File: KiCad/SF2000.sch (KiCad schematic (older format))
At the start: 24 parts, among them J1 Conn_2Rows-86Pins_even_odd, J2 Conn_01x02, U1 LM1117-3.3, U2 TPS73643DBV, U3 SN74CBT16211, U4 SN74CBT16211, U5 SN74CBT16211, U6 SN74AUP1T87DCKR

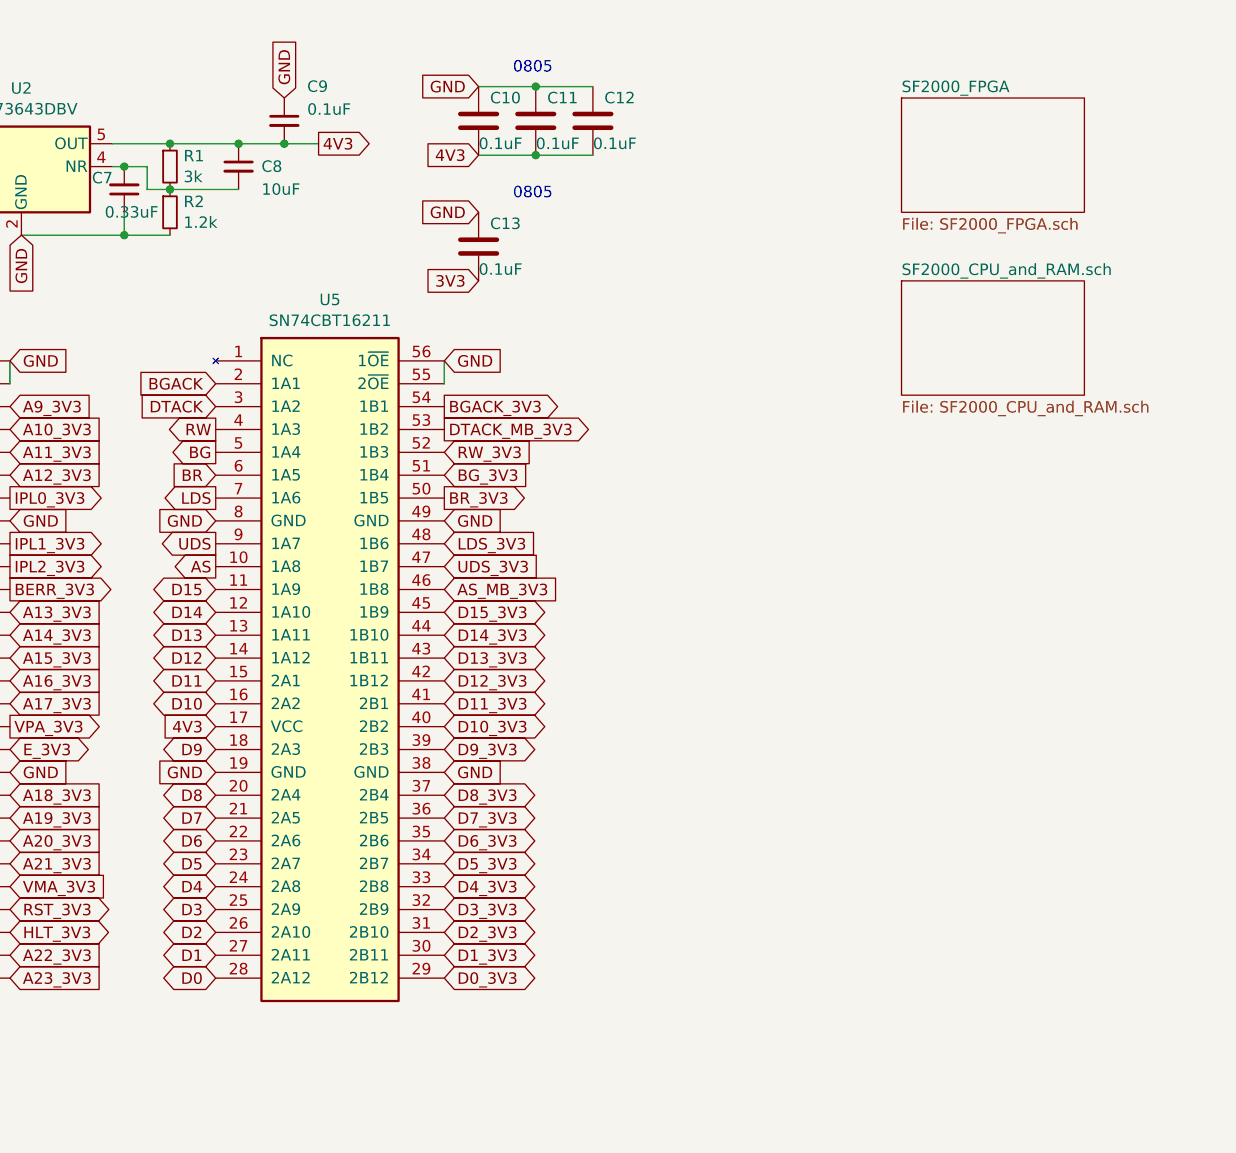
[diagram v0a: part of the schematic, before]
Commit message: reconnected SRAMs and rerouted, and added a lot of caps
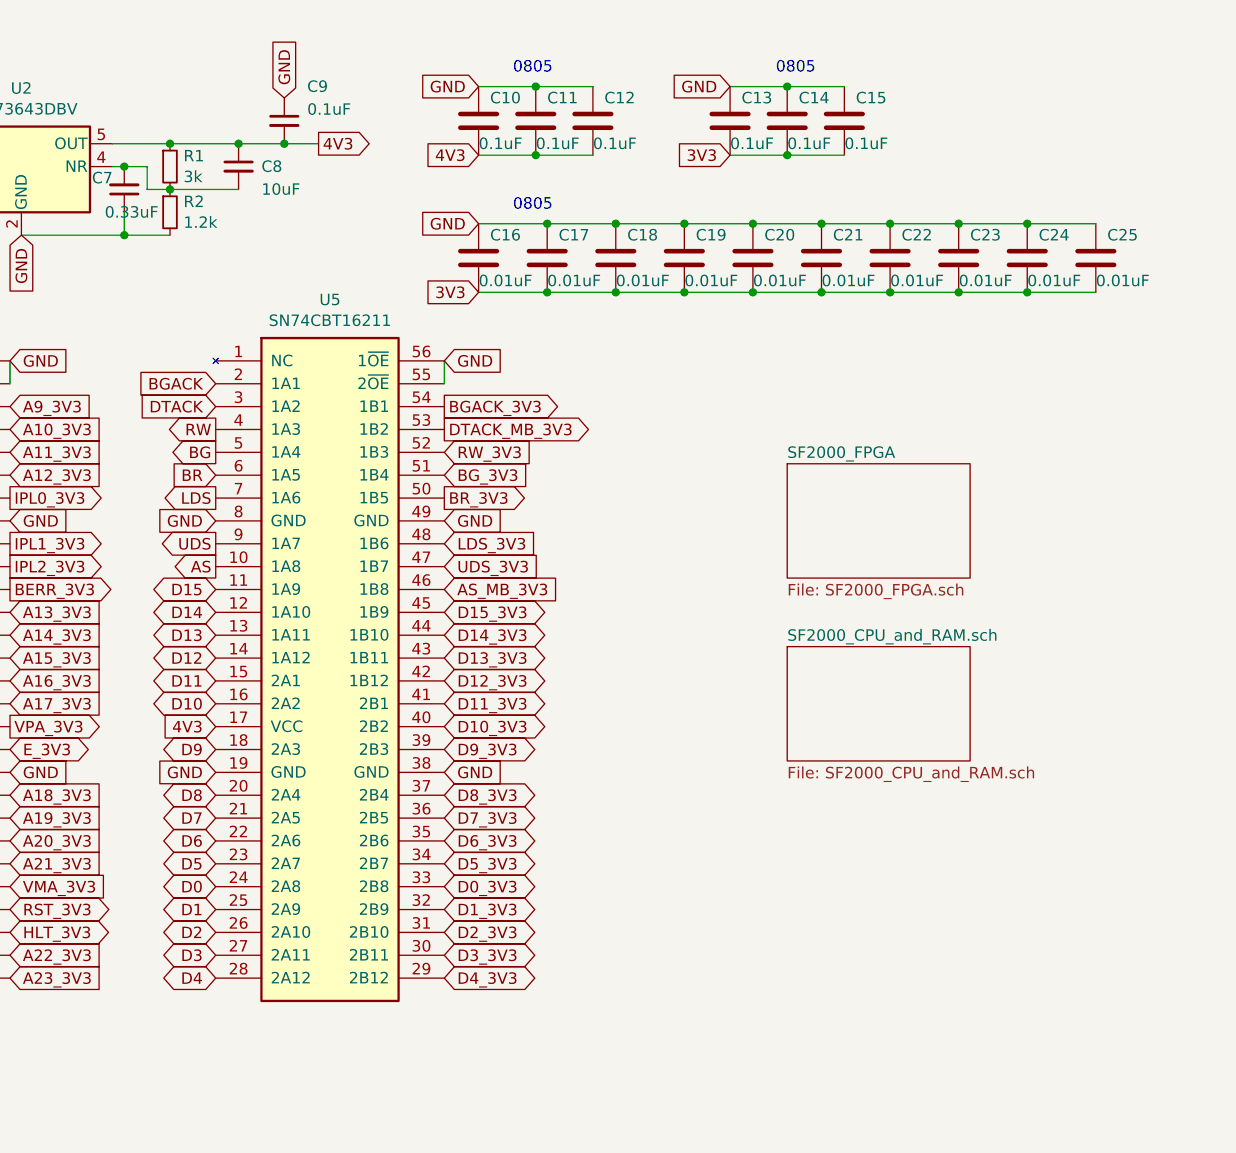
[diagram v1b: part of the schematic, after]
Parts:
- added C14, C15: 0.1uF, Capacitor_SMD:C_0805_2012Metric_Pad1.15x1.40mm_HandSolder, symbol Device:C
- added C16, C17, C18, C19, C20, C21, C22, C23, C24, C25: 0.01uF, Capacitor_SMD:C_0805_2012Metric_Pad1.15x1.40mm_HandSolder, symbol Device:C
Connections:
- net 3V3: now also C14.2, C15.2, C16.2, C17.2, C18.2, C19.2, C20.2, C21.2, C22.2, C23.2, C24.2, C25.2
- net D0: now also U5.24 (2A8); no longer U5.28 (2A12)
- net D0_3V3: now also U5.33 (2B8); no longer U5.29 (2B12)
- net D1: now also U5.25 (2A9); no longer U5.27 (2A11)
- net D1_3V3: now also U5.32 (2B9); no longer U5.30 (2B11)
- net D3: now also U5.27 (2A11); no longer U5.25 (2A9)
- net D3_3V3: now also U5.30 (2B11); no longer U5.32 (2B9)
- net D4: now also U5.28 (2A12); no longer U5.24 (2A8)
- net D4_3V3: now also U5.29 (2B12); no longer U5.33 (2B8)
- net GND: now also C14.1, C15.1, C16.1, C17.1, C18.1, C19.1, C20.1, C21.1, C22.1, C23.1, C24.1, C25.1
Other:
- moved on the sheet: C13
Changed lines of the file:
@@
 Text GLabel 6250 2850 0    50   Output ~ 0
 AS
-Text GLabel 6250 4650 0    50   BiDi ~ 0
+Text GLabel 6250 4250 0    50   BiDi ~ 0
 D0
 Text GLabel 6250 3450 0    50   BiDi ~ 0
 D10
-Text GLabel 6250 4550 0    50   BiDi ~ 0
+Text GLabel 6250 4350 0    50   BiDi ~ 0
 D1
 Text GLabel 6250 3650 0    50   BiDi ~ 0
@@
 Text GLabel 6250 3850 0    50   BiDi ~ 0
 D8
-Text GLabel 6250 4350 0    50   BiDi ~ 0
+Text GLabel 6250 4550 0    50   BiDi ~ 0
 D3
 Text GLabel 6250 3950 0    50   BiDi ~ 0
 D7
-Text GLabel 6250 4250 0    50   BiDi ~ 0
+Text GLabel 6250 4650 0    50   BiDi ~ 0
 D4
 Text GLabel 6250 4050 0    50   BiDi ~ 0
@@
 Text GLabel 2600 5400 0    50   Input ~ 0
 CCK_3V3
-Text GLabel 7400 1300 0    50   Input ~ 0
-GND
-Text GLabel 7400 1600 0    50   Input ~ 0
-3V3
-$Comp
-L Device:C C13
-U 1 1 620B176A
-P 7400 1450
-F 0 "C13" H 7450 1550 50  0000 L CNN
-F 1 "0.1uF" H 7400 1350 50  0000 L CNN
-F 2 "Capacitor_SMD:C_0805_2012Metric_Pad1.15x1.40mm_HandSolder" H 7438 1300 50  0001 C CNN
-F 3 "~" H 7400 1450 50  0001 C CNN
-	1    7400 1450
-	1    0    0    -1
-$EndComp
-Text Notes 7550 1250 0    50   ~ 0
-0805
 NoConn ~ 3550 2150
 NoConn ~ 3550 2250
@@
 CFGOUT_3V3
 $Sheet
-S 9250 800  800  500
+S 8750 2400 800  500
 U 620D263D
 F0 "SF2000_FPGA" 50
@@
 E_3V3
 $Sheet
-S 9250 1600 800  500
+S 8750 3200 800  500
 U 621DFEC4
 F0 "SF2000_CPU_and_RAM.sch" 50
@@
 Text GLabel 7250 2250 2    50   Output ~ 0
 DTACK_MB_3V3
-Text GLabel 7250 4650 2    50   BiDi ~ 0
+Text GLabel 7250 4250 2    50   BiDi ~ 0
 D0_3V3
-Text GLabel 7250 4550 2    50   BiDi ~ 0
+Text GLabel 7250 4350 2    50   BiDi ~ 0
 D1_3V3
 Text GLabel 7250 4450 2    50   BiDi ~ 0
 D2_3V3
-Text GLabel 7250 4350 2    50   BiDi ~ 0
+Text GLabel 7250 4550 2    50   BiDi ~ 0
 D3_3V3
-Text GLabel 7250 4250 2    50   BiDi ~ 0
+Text GLabel 7250 4650 2    50   BiDi ~ 0
 D4_3V3
 Text GLabel 7250 4150 2    50   BiDi ~ 0
@@
 LDS_3V3
 NoConn ~ 3550 3550
+Text Notes 8700 700  0    50   ~ 0
+0805
+Text GLabel 7400 1650 0    50   Input ~ 0
+3V3
+Text GLabel 7400 1350 0    50   Input ~ 0
+GND
+Text GLabel 8500 1050 0    50   Input ~ 0
+3V3
+Text GLabel 8500 750  0    50   Input ~ 0
+GND
+$Comp
+L Device:C C13
+U 1 1 620B176A
+P 8500 900
+F 0 "C13" H 8550 1000 50  0000 L CNN
+F 1 "0.1uF" H 8500 800 50  0000 L CNN
+F 2 "Capacitor_SMD:C_0805_2012Metric_Pad1.15x1.40mm_HandSolder" H 8538 750 50  0001 C CNN
+F 3 "~" H 8500 900 50  0001 C CNN
+	1    8500 900
+	1    0    0    -1
+$EndComp
+Wire Wire Line
+	9200 1650 9500 1650
+Connection ~ 9200 1650
+Wire Wire Line
+	8900 1650 9200 1650
+Connection ~ 8900 1650
+Wire Wire Line
+	8600 1650 8900 1650
+Connection ~ 8600 1650
+Connection ~ 8300 1650
+Wire Wire Line
+	8300 1650 8600 1650
+Wire Wire Line
+	9200 1350 9500 1350
+Connection ~ 9200 1350
+Wire Wire Line
+	8900 1350 9200 1350
+Connection ~ 8900 1350
+Wire Wire Line
+	8600 1350 8900 1350
+Connection ~ 8600 1350
+Connection ~ 8300 1350
+Wire Wire Line
+	8300 1350 8600 1350
+$Comp
+L Device:C C17
+U 1 1 623684C1
+P 7700 1500
+F 0 "C17" H 7750 1600 50  0000 L CNN
+F 1 "0.01uF" H 7700 1400 50  0000 L CNN
+F 2 "Capacitor_SMD:C_0805_2012Metric_Pad1.15x1.40mm_HandSolder" H 7738 1350 50  0001 C CNN
+F 3 "~" H 7700 1500 50  0001 C CNN
+	1    7700 1500
+	1    0    0    -1
+$EndComp
+$Comp
+L Device:C C21
+U 1 1 623684B7
+P 8900 1500
+F 0 "C21" H 8950 1600 50  0000 L CNN
+F 1 "0.01uF" H 8900 1400 50  0000 L CNN
+F 2 "Capacitor_SMD:C_0805_2012Metric_Pad1.15x1.40mm_HandSolder" H 8938 1350 50  0001 C CNN
+F 3 "~" H 8900 1500 50  0001 C CNN
+	1    8900 1500
+	1    0    0    -1
+$EndComp
+$Comp
+L Device:C C20
+U 1 1 623684AD
+P 8600 1500
+F 0 "C20" H 8650 1600 50  0000 L CNN
+F 1 "0.01uF" H 8600 1400 50  0000 L CNN
+F 2 "Capacitor_SMD:C_0805_2012Metric_Pad1.15x1.40mm_HandSolder" H 8638 1350 50  0001 C CNN
+F 3 "~" H 8600 1500 50  0001 C CNN
+	1    8600 1500
+	1    0    0    -1
+$EndComp
+$Comp
+L Device:C C16
+U 1 1 623684A3
+P 7400 1500
+F 0 "C16" H 7450 1600 50  0000 L CNN
+F 1 "0.01uF" H 7400 1400 50  0000 L CNN
+F 2 "Capacitor_SMD:C_0805_2012Metric_Pad1.15x1.40mm_HandSolder" H 7438 1350 50  0001 C CNN
+F 3 "~" H 7400 1500 50  0001 C CNN
+	1    7400 1500
+	1    0    0    -1
+$EndComp
+Wire Wire Line
+	8000 1650 8300 1650
+Connection ~ 8000 1650
+Wire Wire Line
+	7700 1650 8000 1650
+Connection ~ 7700 1650
+Wire Wire Line
+	7400 1650 7700 1650
+Wire Wire Line
+	8000 1350 8300 1350
+Connection ~ 8000 1350
+Wire Wire Line
+	7700 1350 8000 1350
+Connection ~ 7700 1350
+Wire Wire Line
+	7400 1350 7700 1350
+$Comp
+L Device:C C23
+U 1 1 6231D11D
+P 9500 1500
+F 0 "C23" H 9550 1600 50  0000 L CNN
+F 1 "0.01uF" H 9500 1400 50  0000 L CNN
+F 2 "Capacitor_SMD:C_0805_2012Metric_Pad1.15x1.40mm_HandSolder" H 9538 1350 50  0001 C CNN
+F 3 "~" H 9500 1500 50  0001 C CNN
+	1    9500 1500
+	1    0    0    -1
+$EndComp
+$Comp
+L Device:C C22
+U 1 1 6231C987
+P 9200 1500
+F 0 "C22" H 9250 1600 50  0000 L CNN
+F 1 "0.01uF" H 9200 1400 50  0000 L CNN
+F 2 "Capacitor_SMD:C_0805_2012Metric_Pad1.15x1.40mm_HandSolder" H 9238 1350 50  0001 C CNN
+F 3 "~" H 9200 1500 50  0001 C CNN
+	1    9200 1500
+	1    0    0    -1
+$EndComp
+$Comp
+L Device:C C19
+U 1 1 6231BC31
+P 8300 1500
+F 0 "C19" H 8350 1600 50  0000 L CNN
+F 1 "0.01uF" H 8300 1400 50  0000 L CNN
+F 2 "Capacitor_SMD:C_0805_2012Metric_Pad1.15x1.40mm_HandSolder" H 8338 1350 50  0001 C CNN
+F 3 "~" H 8300 1500 50  0001 C CNN
+	1    8300 1500
+	1    0    0    -1
+$EndComp
+Text Notes 7550 1300 0    50   ~ 0
+0805
+$Comp
+L Device:C C18
+U 1 1 623192DF
+P 8000 1500
+F 0 "C18" H 8050 1600 50  0000 L CNN
+F 1 "0.01uF" H 8000 1400 50  0000 L CNN
+F 2 "Capacitor_SMD:C_0805_2012Metric_Pad1.15x1.40mm_HandSolder" H 8038 1350 50  0001 C CNN
+F 3 "~" H 8000 1500 50  0001 C CNN
+	1    8000 1500
+	1    0    0    -1
+$EndComp
+$Comp
+L Device:C C24
+U 1 1 623E0F2C
+P 9800 1500
+F 0 "C24" H 9850 1600 50  0000 L CNN
+F 1 "0.01uF" H 9800 1400 50  0000 L CNN
+F 2 "Capacitor_SMD:C_0805_2012Metric_Pad1.15x1.40mm_HandSolder" H 9838 1350 50  0001 C CNN
+F 3 "~" H 9800 1500 50  0001 C CNN
+	1    9800 1500
+	1    0    0    -1
+$EndComp
+$Comp
+L Device:C C25
+U 1 1 623E1D0B
+P 10100 1500
+F 0 "C25" H 10150 1600 50  0000 L CNN
+F 1 "0.01uF" H 10100 1400 50  0000 L CNN
+F 2 "Capacitor_SMD:C_0805_2012Metric_Pad1.15x1.40mm_HandSolder" H 10138 1350 50  0001 C CNN
+F 3 "~" H 10100 1500 50  0001 C CNN
+	1    10100 1500
+	1    0    0    -1
+$EndComp
+Wire Wire Line
+	9500 1350 9800 1350
+Connection ~ 9500 1350
+Connection ~ 9800 1350
+Wire Wire Line
+	9800 1350 10100 1350
+Wire Wire Line
+	9500 1650 9800 1650
+Connection ~ 9500 1650
+Connection ~ 9800 1650
+Wire Wire Line
+	9800 1650 10100 1650
+$Comp
+L Device:C C14
+U 1 1 623F7CFB
+P 8750 900
+F 0 "C14" H 8800 1000 50  0000 L CNN
+F 1 "0.1uF" H 8750 800 50  0000 L CNN
+F 2 "Capacitor_SMD:C_0805_2012Metric_Pad1.15x1.40mm_HandSolder" H 8788 750 50  0001 C CNN
+F 3 "~" H 8750 900 50  0001 C CNN
+	1    8750 900
+	1    0    0    -1
+$EndComp
+$Comp
+L Device:C C15
+U 1 1 623F86B0
+P 9000 900
+F 0 "C15" H 9050 1000 50  0000 L CNN
+F 1 "0.1uF" H 9000 800 50  0000 L CNN
+F 2 "Capacitor_SMD:C_0805_2012Metric_Pad1.15x1.40mm_HandSolder" H 9038 750 50  0001 C CNN
+F 3 "~" H 9000 900 50  0001 C CNN
+	1    9000 900
+	1    0    0    -1
+$EndComp
+Wire Wire Line
+	8500 750  8750 750
+Connection ~ 8750 750
+Wire Wire Line
+	8750 750  9000 750
+Wire Wire Line
+	8500 1050 8750 1050
+Connection ~ 8750 1050
+Wire Wire Line
+	8750 1050 9000 1050
 $EndSCHEMATC
